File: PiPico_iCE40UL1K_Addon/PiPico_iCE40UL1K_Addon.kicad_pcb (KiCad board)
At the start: 4 copper layers, 21.1 x 51 mm, 29 parts, among them J1 Conn_01x20_Pin, J2 Conn_01x20_Pin, SW1 SW_Push, U1 ICE40LP384-SG32, U2 TLV70033_SOT23-5, U3 TLV70025_SOT23-5, U4 TLV70012_SOT23-5

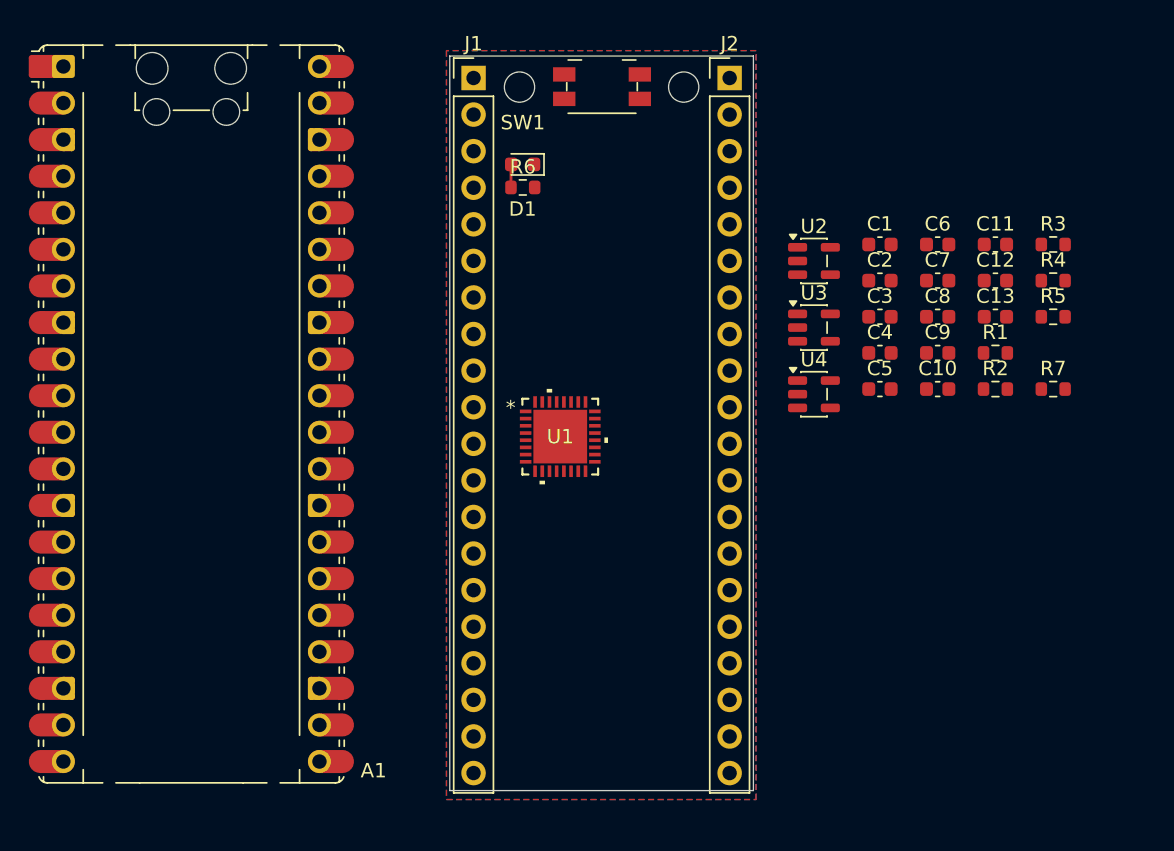
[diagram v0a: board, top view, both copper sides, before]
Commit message: Finished power supply placement and some routing. FPGA power from power supply not routed.
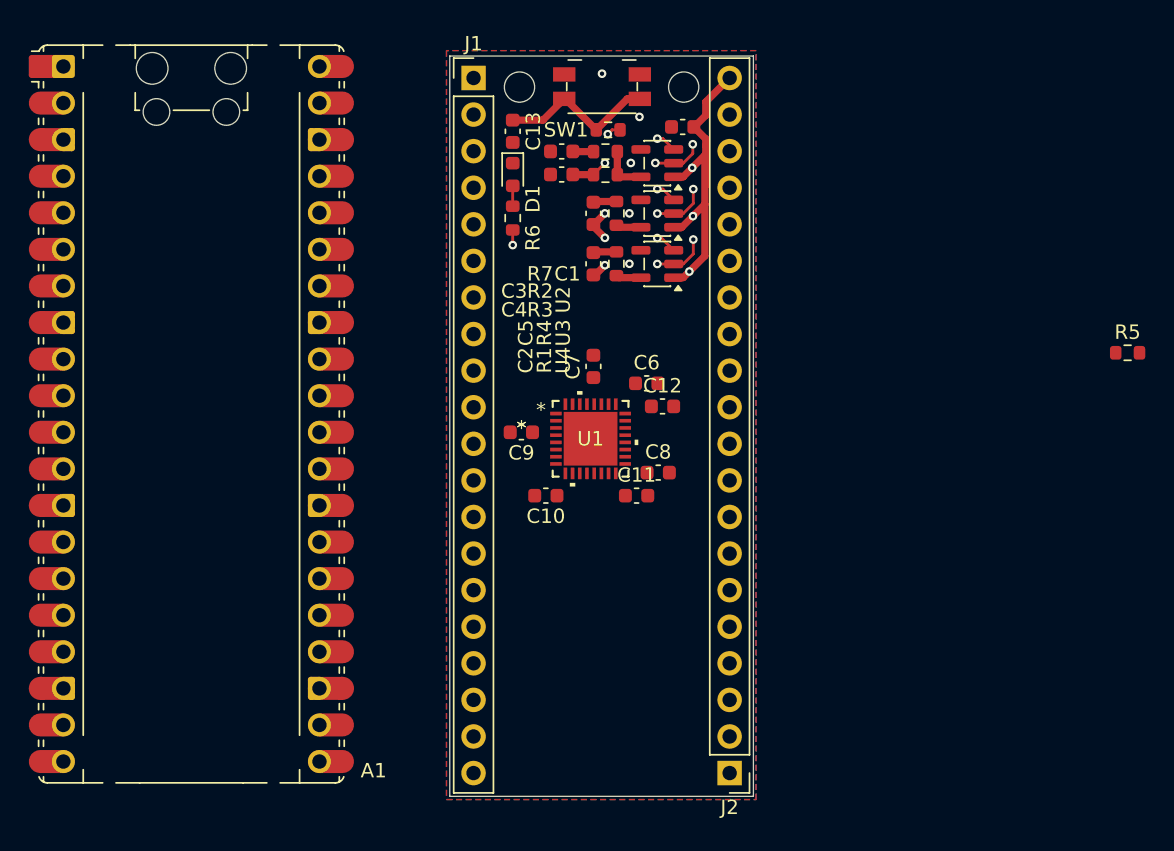
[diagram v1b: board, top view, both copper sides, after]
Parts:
- moved J2 48.3 mm to (124.5, 111.8), turned to 180 degrees
- moved C13 35.9 mm to (109.4, 67.2), turned to -90 degrees
- moved R7 35.8 mm to (116.0, 67.1), turned to 180 degrees
- moved R2 31.7 mm to (115.8, 68.6), turned to 180 degrees
- moved R3 31.5 mm to (115.8, 70.2), turned to 180 degrees
- moved R4 30.7 mm to (116.6, 72.9), turned to 90 degrees
- moved C11 30.4 mm to (118.0, 92.5)
- moved C9 29.4 mm to (110.0, 88.1), turned to 180 degrees
- moved C10 28.2 mm to (111.7, 92.5), turned to 180 degrees
- moved R1 27.0 mm to (116.6, 76.4), turned to 90 degrees
- moved C4 25.3 mm to (112.8, 70.2), turned to 180 degrees
- moved C3 24.9 mm to (112.8, 68.6), turned to 180 degrees
- moved C12 24.7 mm to (119.8, 86.3)
- moved C7 24.6 mm to (115.0, 83.5), turned to 90 degrees
- moved C5 23.3 mm to (115.0, 72.9), turned to -90 degrees
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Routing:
- net /5V0: track 0.00 -> 25.3 mm, vias 0 -> 4
- net /GND: track 0.00 -> 14.6 mm, vias 0 -> 14
- net /CRESET_B: track 0.00 -> 11.2 mm
- net /VCCIO: track 0.00 -> 5.64 mm, vias 0 -> 2
- net /3V3: track 0.00 -> 3.30 mm
- net /2V5: track 0.00 -> 1.76 mm
- net /1V2: track 0.00 -> 1.76 mm
- net /VPP: track 0.00 -> 1.62 mm
- net /VCC: track 0.00 -> 1.62 mm
- net /1V2_EN: track 0.00 -> 1.49 mm, vias 0 -> 1
- net /3V3_EN: track 0.00 -> 1.45 mm, vias 0 -> 1
- net /2V5_EN: track 0.00 -> 1.45 mm, vias 0 -> 1
- net /VCC_SPI: track 0.00 -> 1.44 mm
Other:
- board size 21.1 x 51 mm -> 21.1 x 51.4 mm
- board text added: "*"

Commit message: Finished most of the XIAO floorplan, need to route FPGA caps
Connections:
- U1 pad 33: unconnected-(U1-Pad33) -> /GND
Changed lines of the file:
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@@
 	(net 101 "unconnected-(U1-IOT_53-Pad31)")
 	(net 102 "unconnected-(U1-IOT_50_GBIN1-Pad30)")
-	(net 103 "unconnected-(U1-Pad33)")
-	(net 104 "unconnected-(U1-IOB_26_SCK-Pad15)")
-	(net 105 "unconnected-(U1-IOR_35_GBIN3-Pad19)")
-	(net 106 "unconnected-(U1-IOL_2A-Pad2)")
+	(net 103 "unconnected-(U1-IOB_26_SCK-Pad15)")
+	(net 104 "unconnected-(U1-IOR_35_GBIN3-Pad19)")
+	(net 105 "unconnected-(U1-IOL_2A-Pad2)")
 	(footprint "Resistor_SMD:R_0603_1608Metric"
 		(layer "F.Cu")
@@
 			(size 0.254 0.8048)
 			(layers "F.Cu" "F.Mask" "F.Paste")
-			(net 106 "unconnected-(U1-IOL_2A-Pad2)")
+			(net 105 "unconnected-(U1-IOL_2A-Pad2)")
 			(pinfunction "IOL_2A")
 			(pintype "bidirectional")
@@
 			(size 0.254 0.8048)
 			(layers "F.Cu" "F.Mask" "F.Paste")
-			(net 104 "unconnected-(U1-IOB_26_SCK-Pad15)")
+			(net 103 "unconnected-(U1-IOB_26_SCK-Pad15)")
 			(pinfunction "IOB_26_SCK")
 			(pintype "bidirectional")
@@
 			(size 0.254 0.8048)
 			(layers "F.Cu" "F.Mask" "F.Paste")
-			(net 105 "unconnected-(U1-IOR_35_GBIN3-Pad19)")
+			(net 104 "unconnected-(U1-IOR_35_GBIN3-Pad19)")
 			(pinfunction "IOR_35_GBIN3")
 			(pintype "bidirectional")
@@
 			(size 3.7338 3.7338)
 			(layers "F.Cu" "F.Mask" "F.Paste")
-			(net 103 "unconnected-(U1-Pad33)")
+			(net 36 "/GND")
 			(pinfunction "33")
 			(pintype "unspecified")
